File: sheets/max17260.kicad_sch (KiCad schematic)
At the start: 0 parts

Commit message: More cleanup
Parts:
- added U3: MAX17260, symbol PowerFeather_KiCAD_Lib:MAX17260
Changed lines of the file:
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@@
 	(generator "eeschema")
 	(generator_version "8.0")
-	(paper "A4")
+	(paper "A5")
 	(hierarchical_label "VBAT"
 		(shape input)
-		(at 138.43 86.36 0)
+		(at 97.79 45.72 0)
 		(fields_autoplaced yes)
 		(effects
@@
 	(hierarchical_label "GND"
 		(shape input)
-		(at 139.7 95.25 0)
+		(at 99.06 54.61 0)
 		(fields_autoplaced yes)
 		(effects
@@
 	(hierarchical_label "SCL"
 		(shape bidirectional)
-		(at 170.18 105.41 0)
+		(at 129.54 64.77 0)
 		(fields_autoplaced yes)
 		(effects
@@
 	(hierarchical_label "SDA"
 		(shape bidirectional)
-		(at 170.18 110.49 0)
+		(at 129.54 69.85 0)
 		(fields_autoplaced yes)
 		(effects
@@
 	(hierarchical_label "ALARM"
 		(shape output)
-		(at 170.18 99.06 0)
+		(at 129.54 58.42 0)
 		(fields_autoplaced yes)
 		(effects
@@
 		)
 	)
+	(symbol
+		(lib_id "PowerFeather_KiCAD_Lib:MAX17260")
+		(at 74.93 77.47 0)
+		(unit 1)
+		(exclude_from_sim no)
+		(in_bom yes)
+		(on_board yes)
+		(dnp no)
+		(fields_autoplaced yes)
+		(property "Reference" "U3"
+			(at 74.93 88.9 0)
+			(effects
+				(font
+					(size 1.27 1.27)
+				)
+			)
+		)
+		(property "Value" "MAX17260"
+			(at 74.93 91.44 0)
+			(effects
+				(font
+					(size 1.27 1.27)
+				)
+			)
+		)
+		(property "Footprint" ""
+			(at 74.93 88.138 0)
+			(effects
+				(font
+					(size 1.27 1.27)
+				)
+				(hide yes)
+			)
+		)
+		(property "Datasheet" ""
+			(at 74.168 90.678 0)
+			(effects
+				(font
+					(size 1.27 1.27)
+				)
+				(hide yes)
+			)
+		)
+		(property "Description" ""
+			(at 74.93 77.47 0)
+			(effects
+				(font
+					(size 1.27 1.27)
+				)
+				(hide yes)
+			)
+		)
+		(pin "C3"
+		)
+		(pin "A1"
+		)
+		(pin "B3"
+		)
+		(pin "B1"
+		)
+		(pin "A2"
+		)
+		(pin "C1"
+		)
+		(pin "B2"
+		)
+		(pin "A3"
+		)
+		(pin "C2"
+		)
+		(instances
+			(project ""
+				(path "/5be6a852-fa78-49fa-bb8c-8d5ad39f4b26/46173bec-ea31-4af7-a417-264e4953a5cb/b14ae25c-1044-42b2-88e6-486f3cf2e161"
+					(reference "U3")
+					(unit 1)
+				)
+			)
+		)
+	)

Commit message: More cleanup
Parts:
- renumbered U3 to U6
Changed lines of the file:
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@@
 		(dnp no)
 		(fields_autoplaced yes)
-		(property "Reference" "U3"
+		(property "Reference" "U6"
 			(at 74.93 88.9 0)
 			(effects
@@
 		)
 		(instances
-			(project ""
-				(path "/5be6a852-fa78-49fa-bb8c-8d5ad39f4b26/46173bec-ea31-4af7-a417-264e4953a5cb/b14ae25c-1044-42b2-88e6-486f3cf2e161"
-					(reference "U3")
+			(project "esp32s3-powerfeather"
+				(path "/5be6a852-fa78-49fa-bb8c-8d5ad39f4b26/a940761a-0d45-4491-ba89-ec093a8f239f/b14ae25c-1044-42b2-88e6-486f3cf2e161"
+					(reference "U6")
 					(unit 1)
 				)

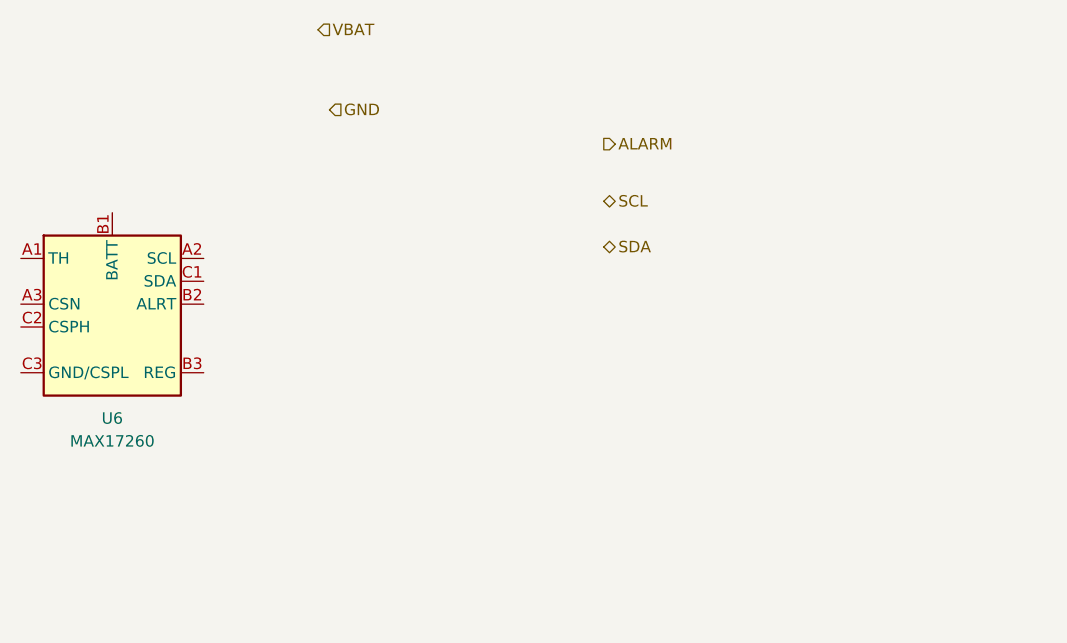
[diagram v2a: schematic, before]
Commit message: Fix max17260 schematic
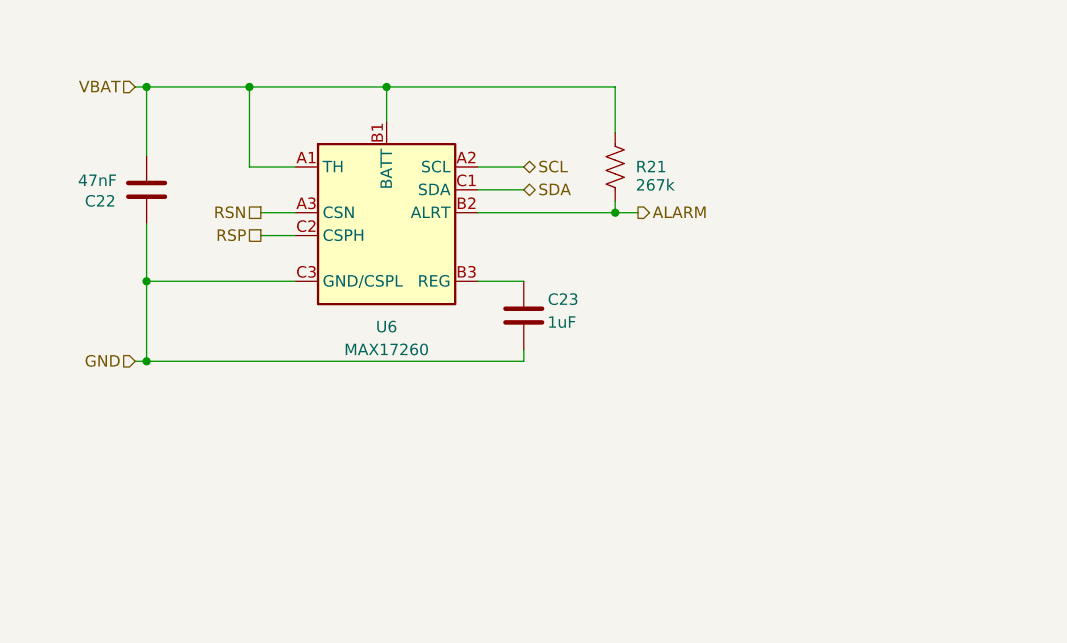
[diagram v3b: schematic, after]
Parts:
- added C22: 47nF, Capacitor_SMD:C_0402_1005Metric, symbol Device:C
- added C23: 1uF, Capacitor_SMD:C_0402_1005Metric, symbol Device:C
- added R21: 267k, Resistor_SMD:R_0402_1005Metric, symbol Device:R_US
- U6: footprint (none) -> Package_BGA:WLP-9_1.448x1.468mm_Layout3x3_P0.4mm_Ball0.27mm_Pad0.25mm
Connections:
- net ALARM: now also U6.B2 (ALRT), R21.2
- net GND: now also U6.C3 (GND/CSPL), C22.2, C23.2
- net SCL: now also U6.A2 (SCL)
- net SDA: now also U6.C1 (SDA)
- net VBAT: now also U6.A1 (TH), U6.B1 (BATT), C22.1, R21.1
- net RSN: now reaches U6.A3 (CSN)
- net at U6.B3 (REG): now also C23.1
- net RSP: now reaches U6.C2 (CSPH)
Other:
- moved on the sheet: U6
